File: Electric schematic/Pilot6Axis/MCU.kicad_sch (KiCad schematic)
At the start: 26 parts, among them J10 BTN5, J11 BTN6, J12 BTN7, J13 BTN8, J14 BTN9, J15 BTN10, J16 BTN11, J19 Conn_02x03_Odd_Even, J3 Conn_02x03_Odd_Even, J5 Oled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

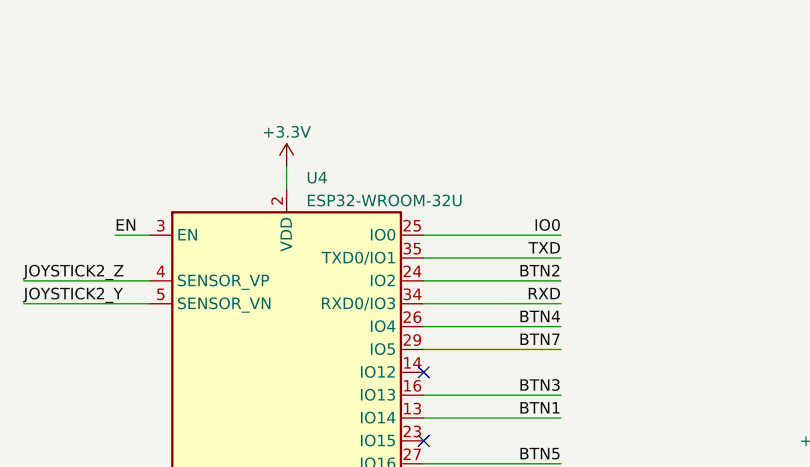
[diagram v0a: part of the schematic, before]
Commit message: update schematic to kicajd 9.0,    fixed usb D=/D- wrongly inerconnected , otherwise pcb seems to be woekring
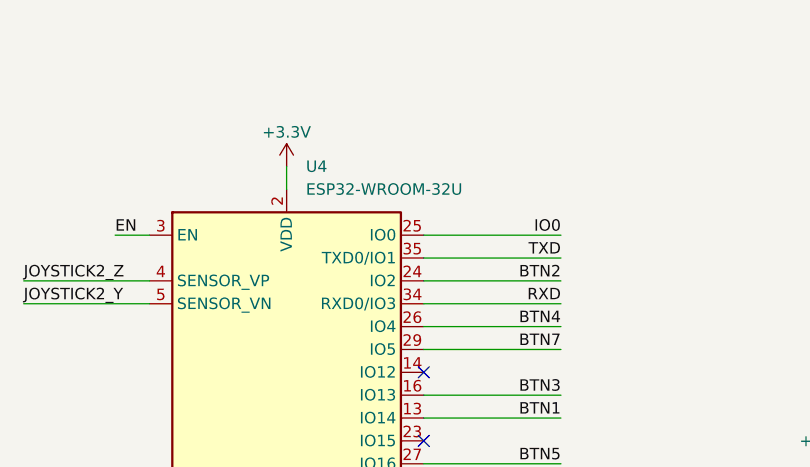
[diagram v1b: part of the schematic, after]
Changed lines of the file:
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@@
 (kicad_sch
-	(version 20231120)
+	(version 20250114)
 	(generator "eeschema")
-	(generator_version "8.0")
+	(generator_version "9.0")
 	(paper "A4")
+	(rectangle
+		(start 198.12 63.5)
+		(end 246.38 85.09)
+		(stroke
+			(width 0)
+			(type dash)
+		)
+		(fill
+			(type none)
+		)
+	)
+	(rectangle
+		(start 246.38 110.49)
+		(end 284.48 162.56)
+		(stroke
+			(width 0)
+			(type dash)
+		)
+		(fill
+			(type none)
+		)
+	)
+	(rectangle
+		(start 246.38 13.97)
+		(end 284.48 110.49)
+		(stroke
+			(width 0)
+			(type dash)
+		)
+		(fill
+			(type none)
+		)
+	)
+	(rectangle
+		(start 198.12 13.97)
+		(end 246.38 63.5)
+		(stroke
+			(width 0)
+			(type dash)
+		)
+		(fill
+			(type none)
+		)
+	)
+	(text "Buttons input\nBOTOM"
+		(exclude_from_sim no)
+		(at 266.446 115.824 0)
+		(effects
+			(font
+				(size 1.27 1.27)
+			)
+			(justify bottom)
+		)
+	)
+	(text "Buttons input\nFRONT"
+		(exclude_from_sim no)
+		(at 266.7 20.828 0)
+		(effects
+			(font
+				(size 1.27 1.27)
+			)
+			(justify bottom)
+		)
+	)
+	(text "Joystick input"
+		(exclude_from_sim no)
+		(at 215.138 16.51 0)
+		(effects
+			(font
+				(size 1.27 1.27)
+			)
+			(justify left bottom)
+		)
+	)
+	(text "OLED connector"
+		(exclude_from_sim no)
+		(at 229.362 66.548 0)
+		(effects
+			(font
+				(size 1.27 1.27)
+			)
+			(justify right bottom)
+		)
+	)
 	(junction
 		(at 35.56 52.07)
@@
 		)
 	)
-	(rectangle
-		(start 198.12 63.5)
-		(end 246.38 85.09)
-		(stroke
-			(width 0)
-			(type dash)
-		)
-		(fill
-			(type none)
-		)
-	)
-	(rectangle
-		(start 246.38 110.49)
-		(end 284.48 162.56)
-		(stroke
-			(width 0)
-			(type dash)
-		)
-		(fill
-			(type none)
-		)
-	)
-	(rectangle
-		(start 246.38 13.97)
-		(end 284.48 110.49)
-		(stroke
-			(width 0)
-			(type dash)
-		)
-		(fill
-			(type none)
-		)
-	)
-	(rectangle
-		(start 198.12 13.97)
-		(end 246.38 63.5)
-		(stroke
-			(width 0)
-			(type dash)
-		)
-		(fill
-			(type none)
-		)
-	)
-	(text "Buttons input\nBOTOM"
-		(exclude_from_sim no)
-		(at 266.446 115.824 0)
-		(effects
-			(font
-				(size 1.27 1.27)
-			)
-			(justify bottom)
-		)
-	)
-	(text "Buttons input\nFRONT"
-		(exclude_from_sim no)
-		(at 266.7 20.828 0)
-		(effects
-			(font
-				(size 1.27 1.27)
-			)
-			(justify bottom)
-		)
-	)
-	(text "Joystick input"
-		(exclude_from_sim no)
-		(at 215.138 16.51 0)
-		(effects
-			(font
-				(size 1.27 1.27)
-			)
-			(justify left bottom)
-		)
-	)
-	(text "OLED connector"
-		(exclude_from_sim no)
-		(at 229.362 66.548 0)
-		(effects
-			(font
-				(size 1.27 1.27)
-			)
-			(justify right bottom)
-		)
-	)
 	(label "JOYSTICK2_Y"
 		(at 242.57 50.8 180)
@@
 		(fields_autoplaced yes)
 		(property "Reference" "U4"
-			(at 120.3041 31.75 0)
+			(at 120.2533 30.48 0)
 			(effects
 				(font
@@
 		)
 		(property "Value" "ESP32-WROOM-32U"
-			(at 120.3041 34.29 0)
+			(at 120.2533 33.02 0)
 			(effects
 				(font

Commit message: upgrade board to use USB BD for power delivery and addded SPI screen conector
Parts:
- removed J15: BTN10, Connector_Molex:Molex_KK-254_AE-6410-02A_1x02_P2.54mm_Vertical, symbol molex-2pin:22-27-2021
- removed J16: BTN11, Connector_Molex:Molex_KK-254_AE-6410-02A_1x02_P2.54mm_Vertical, symbol molex-2pin:22-27-2021
- added J16: Oled, Connector_PinSocket_2.54mm:PinSocket_2x03_P2.54mm_Vertical, symbol Connector_Generic:Conn_02x03_Odd_Even
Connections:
- net BTN10 is gone; now on net BTN3: U4.11 (IO26)
- net BTN11 is gone; now on net BTN1: U4.12 (IO27)
- net +3.3V: now also J16.4 (Pin_4)
- net BTN1: no longer U4.13 (IO14)
- net BTN3: no longer U4.16 (IO13)
- net GND: now also J16.6 (Pin_6)
- net MISO: now reaches U4.14 (IO12)
- net MISO: now also J16.1 (Pin_1)
- net CS: now reaches U4.23 (IO15)
- net CS: now also J16.2 (Pin_2)
- new net MCLK: J16.5 (Pin_5), U4.13 (IO14)
- new net MOSI: J16.3 (Pin_3), U4.16 (IO13)
- no-connect marks 8 -> 6

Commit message: fixed leyout
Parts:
- removed C13: 1nF, Capacitor_SMD:C_0603_1608Metric, symbol Device:C
- removed R13, R14: 470R, Resistor_SMD:R_0603_1608Metric, symbol Device:R
- added R13, R26: 22Ω, PCM_JLCPCB:R_0603, symbol PCM_JLCPCB-Resistors:0603,22Ω
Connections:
- net EN: now also R13.2
- net IO0: now also C14.2, R26.2
- net at SW2.2: now also R26.1; no longer C14.2
- net at SW1.2: now also R13.1
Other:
- moved on the sheet: C14
